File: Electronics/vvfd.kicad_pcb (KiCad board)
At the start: 2 copper layers, 95 x 95 mm, 70 parts, among them J1 USB_C_Receptacle_USB2.0_14P, J2 Conn_01x02_Pin, J3 Conn_02x05_Counter_Clockwise, J4 Conn_02x05_Counter_Clockwise, J5 Conn_02x05_Counter_Clockwise, J6 Conn_01x08_Pin, J7 Conn_01x08_Pin, J8 Conn_01x08_Pin, J9 Conn_01x08_Pin, Q1 RFD14N05L, Q2 RFD14N05L, Q3 RFD14N05L, Q4 RFD14N05L, Q5 RFD14N05L, Q6 RFD14N05L, U1 MC34063AD, U10 TBD62783A, U2 TLV274, U3 74HC595, U4 TBD62783A, U5 74HC595, U6 TBD62783A, U7 74HC595, U8 TBD62783A, U9 74HC595

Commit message: Fixed ERC and DRC
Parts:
- Q1, Q2, Q3, Q4, Q5, Q6: value RFD14N05L -> IRLU014PBF

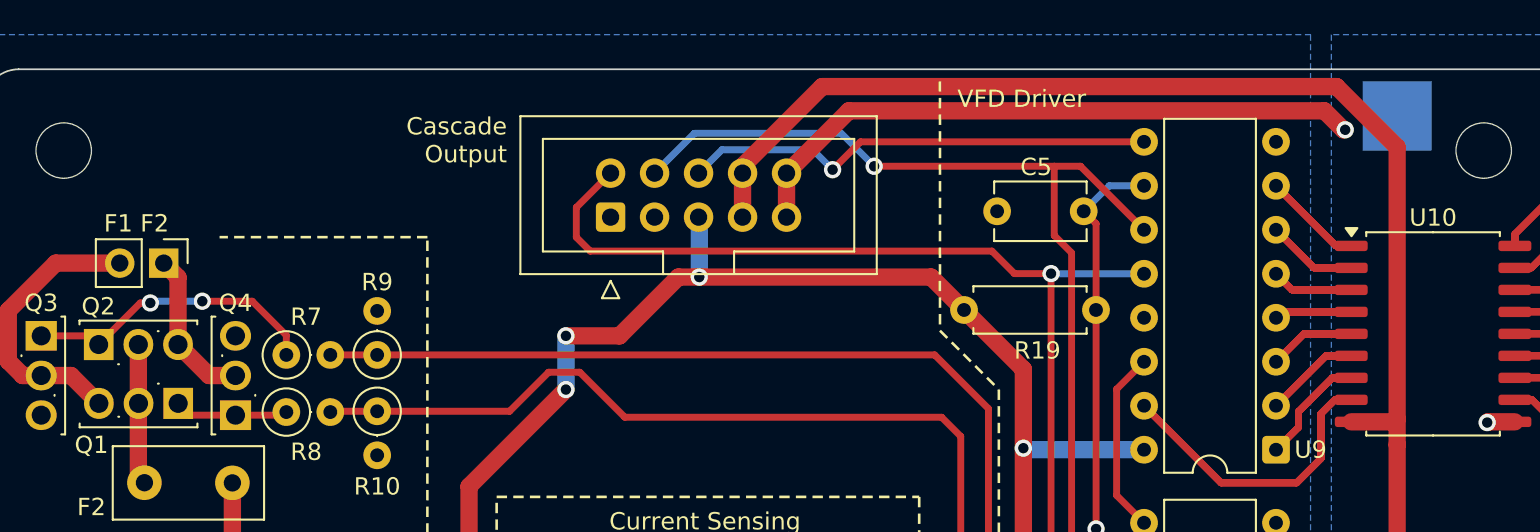
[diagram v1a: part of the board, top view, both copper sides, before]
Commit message: Fix cascade IDC connector
The cascade input and output IDC pins didn't correspond before
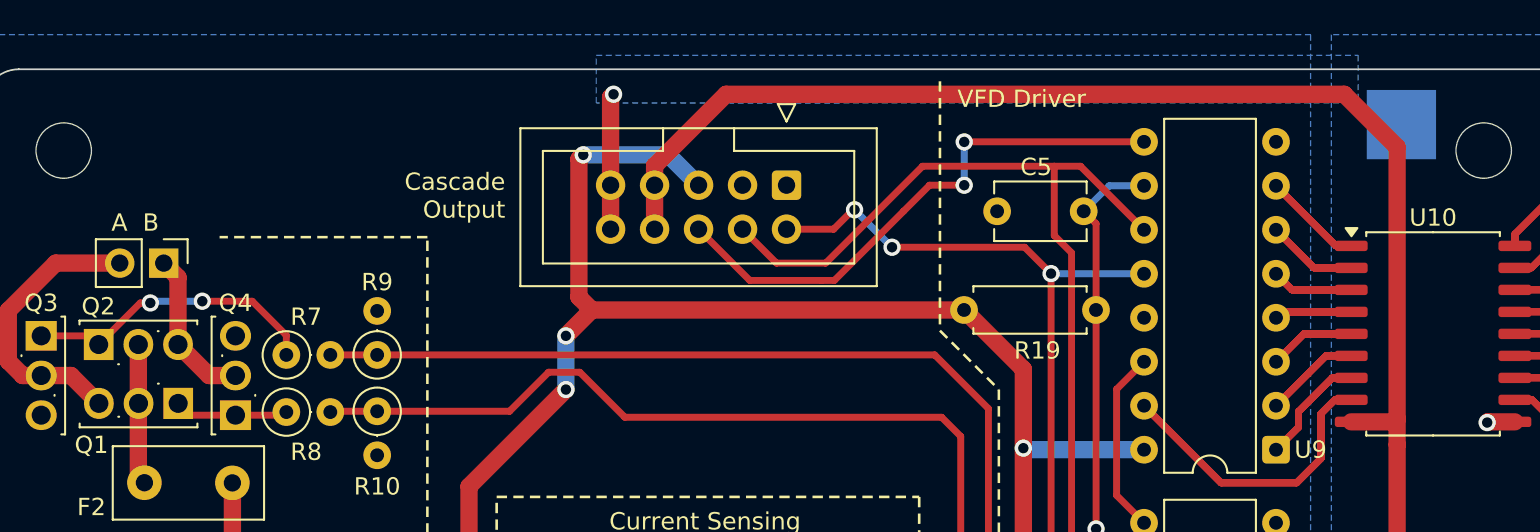
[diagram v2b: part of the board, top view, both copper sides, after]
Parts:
- moved J3 10.3 mm to (159.7, 50.0), turned to -90 degrees
- moved TP3 0.56 mm to (195.2, 46.5)
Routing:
- net GNDA: track 154.4 -> 125.5 mm
- net SYNC: track 155.5 -> 139.9 mm, vias 1 -> 3
- net VCC: track 204.5 -> 216.2 mm
- net VDC: track 232.5 -> 237.7 mm
- net MAIN_SER_OUT: track 27.4 -> 31.7 mm, vias 1 -> 2
- net CLK: track 152.3 -> 148.6 mm, vias 7 -> 6
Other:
- board text added: "A B"
- board text removed: "F1 F2"

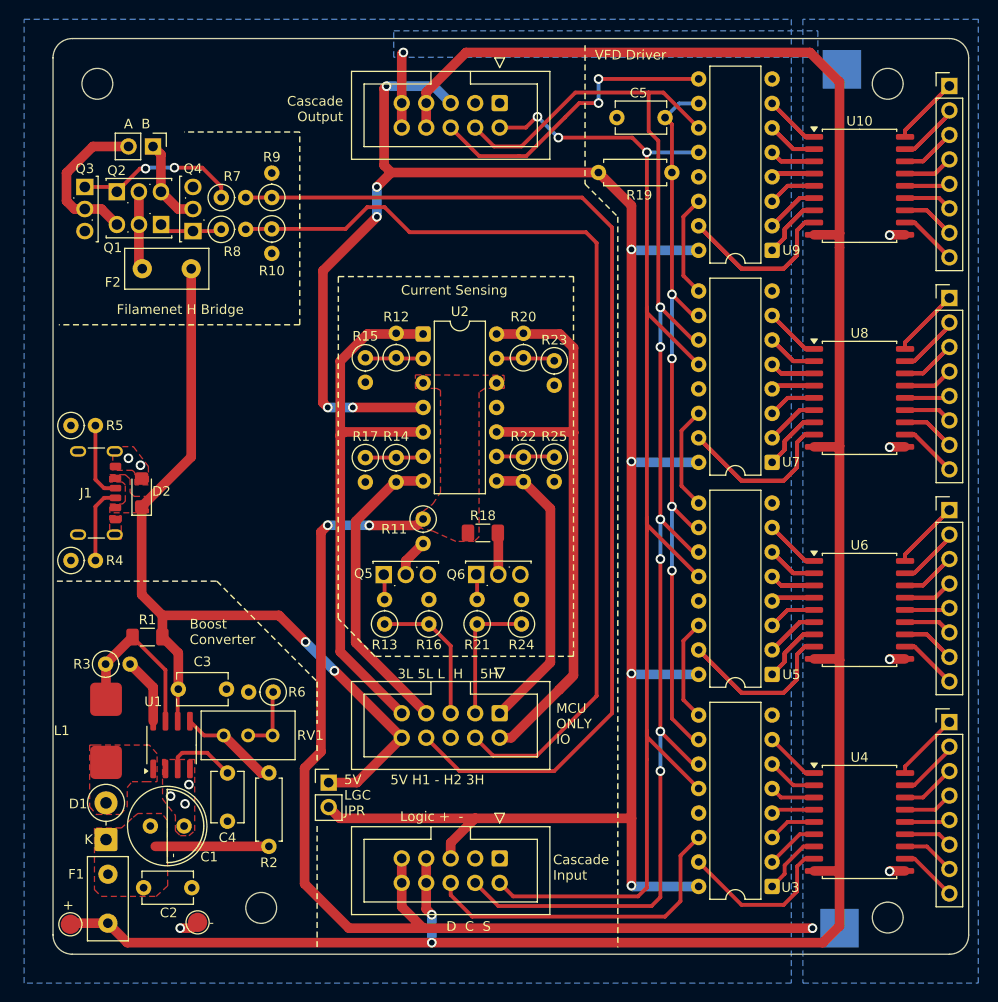
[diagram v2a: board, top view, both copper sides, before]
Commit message: Added filament timer
Added a timer to control the filament h-brdige on the main PCB.
Also added some more decoupling capacitors, but some have dubious
placement. Still better than nothing.
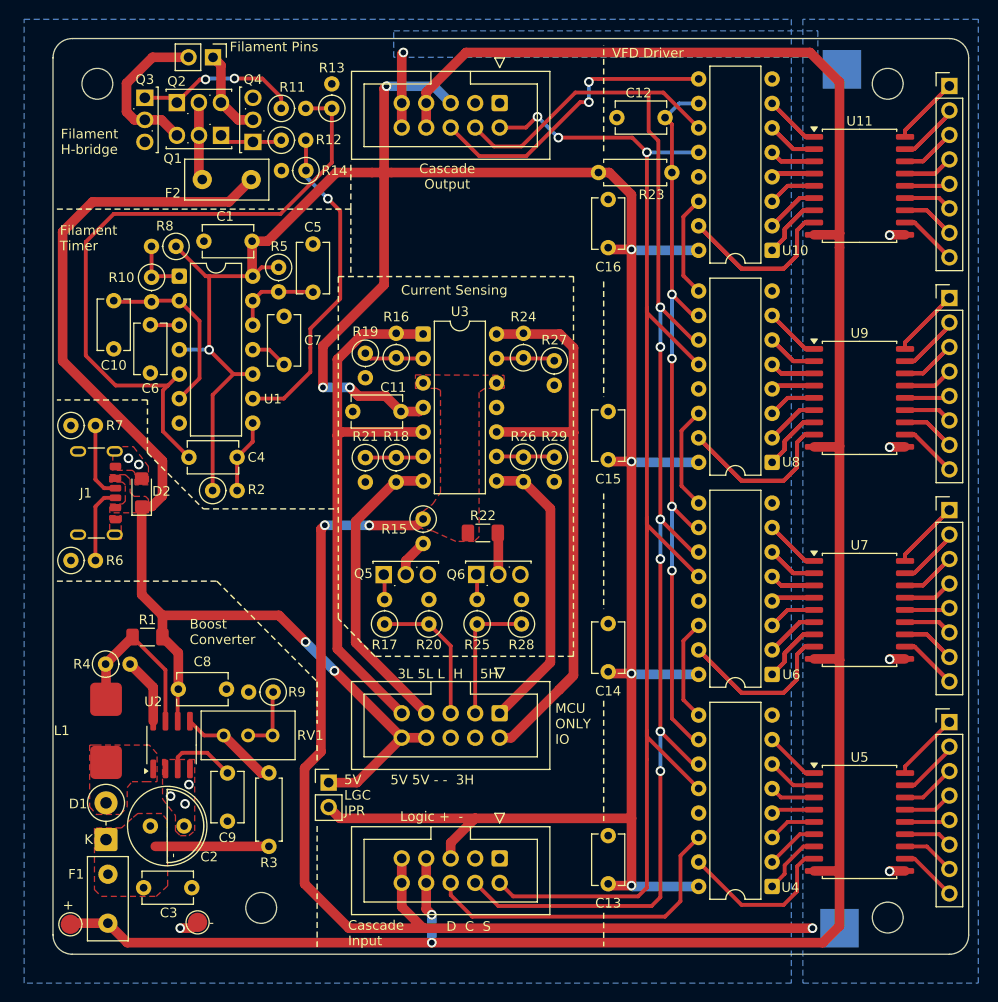
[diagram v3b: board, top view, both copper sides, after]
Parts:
- added C1: 100n, Capacitor_THT:C_Disc_D5.1mm_W3.2mm_P5.00mm, F.Cu at (134.1, 64.3)
- added C10: 220n, Capacitor_THT:C_Disc_D5.1mm_W3.2mm_P5.00mm, F.Cu at (119.7, 70.5)
- added C11: 100n, Capacitor_THT:C_Disc_D5.1mm_W3.2mm_P5.00mm, F.Cu at (149.5, 82.0)
- added C13: 100n, Capacitor_THT:C_Disc_D5.1mm_W3.2mm_P5.00mm, F.Cu at (171.0, 131.0)
- added C14: 100n, Capacitor_THT:C_Disc_D5.1mm_W3.2mm_P5.00mm, F.Cu at (171.0, 109.0)
- added C15: 100n, Capacitor_THT:C_Disc_D5.1mm_W3.2mm_P5.00mm, F.Cu at (171.0, 87.0)
- added C16: 100n, Capacitor_THT:C_Disc_D5.1mm_W3.2mm_P5.00mm, F.Cu at (171.0, 65.0)
- added C4: 1n, Capacitor_THT:C_Disc_D5.1mm_W3.2mm_P5.00mm, F.Cu at (127.5, 86.8)
- added C5: 220n, Capacitor_THT:C_Disc_D5.1mm_W3.2mm_P5.00mm, F.Cu at (140.4, 69.6)
- added C6: 10n, Capacitor_THT:C_Disc_D5.1mm_W3.2mm_P5.00mm, F.Cu at (123.5, 73.0)
- added C7: 10n, Capacitor_THT:C_Disc_D5.1mm_W3.2mm_P5.00mm, F.Cu at (137.4, 77.1)
- added R10: 68k, Resistor_THT:R_Axial_DIN0207_L6.3mm_D2.5mm_P2.54mm_Vertical, F.Cu at (123.6, 68.1)
- added R2: 33k, Resistor_THT:R_Axial_DIN0207_L6.3mm_D2.5mm_P2.54mm_Vertical, F.Cu at (130.0, 90.2)
- added R5: 39k, Resistor_THT:R_Axial_DIN0207_L6.3mm_D2.5mm_P2.54mm_Vertical, F.Cu at (136.8, 67.0)
- added R8: 1k, Resistor_THT:R_Axial_DIN0207_L6.3mm_D2.5mm_P2.54mm_Vertical, F.Cu at (126.2, 64.9)
- added U1: LM556, Package_DIP:DIP-14_W7.62mm, F.Cu at (126.5, 68.0)
- moved R11 11.1 mm to (137.1, 50.5)
- moved R12 11.1 mm to (137.1, 53.9)
- moved F2 11.1 mm to (134.0, 57.9)
- moved Q1 11.1 mm to (130.8, 53.4)
- moved Q2 11.1 mm to (126.2, 50.0)
- moved Q4 11.1 mm to (134.1, 54.0)
- moved J2 11.1 mm to (130.0, 45.2)
- moved Q3 11.1 mm to (122.9, 49.5)
- moved R13 11.1 mm to (142.3, 50.5)
- moved R14 7.02 mm to (139.6, 57.0), turned to 180 degrees
- moved R19 0.47 mm to (145.8, 76.0)
- renumbered C5 to C12, C1 to C2, C2 to C3, C3 to C8, C4 to C9, J5 to J4, J4 to J5, R7 to R11, R8 to R12, R9 to R13, R10 to R14, R11 to R15, R12 to R16, R13 to R17, R14 to R18, R15 to R19, R16 to R20, R17 to R21, R18 to R22, R19 to R23, R20 to R24, R21 to R25, R22 to R26, R23 to R27, R24 to R28, R25 to R29, R2 to R3, R3 to R4, R4 to R6, R5 to R7, R6 to R9, TP3 to TP1, TP4 to TP2, TP2 to TP3, TP1 to TP4, U9 to U10, U10 to U11, U1 to U2, U2 to U3, U3 to U4, U4 to U5, U5 to U6, U6 to U7, U7 to U8, U8 to U9
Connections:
- J4 pad 4: H2 -> GND
- J4 pad 8: H1 -> +5V
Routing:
- net VCC: track 216.2 -> 288.3 mm, vias 9 -> 8
- net H2: track 101.8 -> 34.0 mm, vias 0 -> 1
- net H1: track 112.9 -> 69.3 mm
- net +5V: track 90.5 -> 122.3 mm
- net /TIMING_CAP_1: track 0.00 -> 18.8 mm
- net /TIMING_CAP_2: track 0.00 -> 9.19 mm
- net /TIM_2_IN: track 0.00 -> 7.67 mm
- net /TIM_1_DIS: track 0.00 -> 6.13 mm
- net /TIM_2_CV: track 0.00 -> 3.89 mm
- net /TIM_1_CV: track 0.00 -> 3.02 mm
- net 3LCS: track 57.8 -> 58.6 mm
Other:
- board text added: "5V 5V - - 3H"
- board text added: "Filament H-bridge"
- board text added: "Filament Pins"
- board text added: "Filament Timer"
- board text removed: "5V H1 - H2 3H"
- board text removed: "A B"
- board text removed: "Filamenet H Bridge"

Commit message: Added VFD output pulldowns
Added pulldowns and more decoupling capacitors. The capacitors and
pulldowns can probably be omitted, but I've put them in for more flexibility.
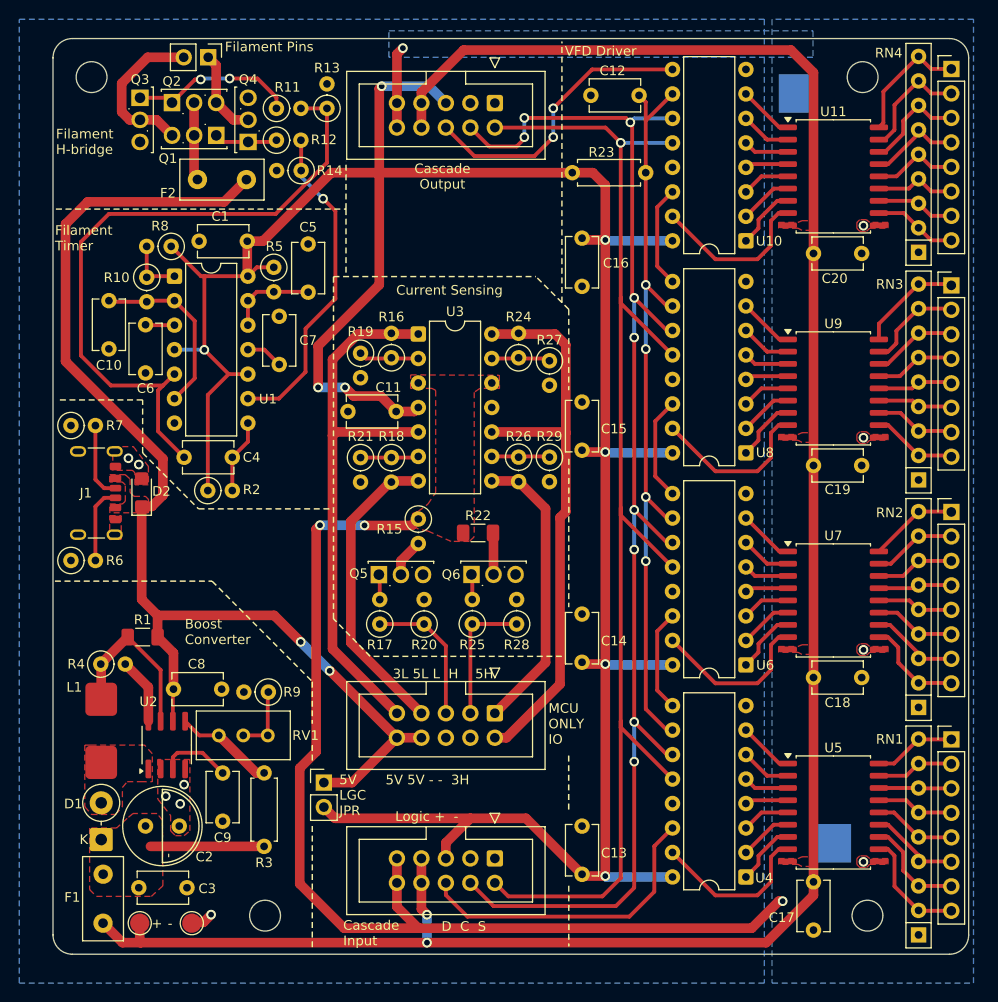
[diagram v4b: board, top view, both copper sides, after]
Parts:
- added C17: 100n, Capacitor_THT:C_Disc_D5.1mm_W3.2mm_P5.00mm, F.Cu at (192.3, 130.8)
- added C18: 100n, Capacitor_THT:C_Disc_D5.1mm_W3.2mm_P5.00mm, F.Cu at (192.3, 109.6)
- added C19: 100n, Capacitor_THT:C_Disc_D5.1mm_W3.2mm_P5.00mm, F.Cu at (192.3, 87.6)
- added C20: 100n, Capacitor_THT:C_Disc_D5.1mm_W3.2mm_P5.00mm, F.Cu at (192.3, 65.6)
- added RN1: 1M, Resistor_THT:R_Array_SIP9, F.Cu at (203.2, 136.3)
- added RN2: 1M, Resistor_THT:R_Array_SIP9, F.Cu at (203.2, 112.7)
- added RN3: 1M, Resistor_THT:R_Array_SIP9, F.Cu at (203.2, 89.1)
- added RN4: 1M, Resistor_THT:R_Array_SIP9, F.Cu at (203.2, 65.5)
- moved TP2 8.84 mm to (194.2, 126.8)
- moved TP4 7.20 mm to (122.4, 135.1)
- moved TP1 5.19 mm to (190.7, 49.0)
- moved C12 3.55 mm to (174.2, 49.2)
- moved C13 2.89 mm to (168.3, 130.0)
- moved U4 2.89 mm to (185.3, 130.3)
- moved C14 2.89 mm to (168.3, 108.0)
- moved C15 2.89 mm to (168.3, 86.0)
- moved C16 2.89 mm to (168.3, 64.0), turned to -90 degrees
- moved U10 2.89 mm to (185.3, 64.3)
- moved U6 2.89 mm to (185.3, 108.3)
- moved U8 2.89 mm to (185.3, 86.3)
- moved U11 2.89 mm to (194.4, 57.6)
- moved U5 2.89 mm to (194.4, 123.6)
- moved U7 2.89 mm to (194.4, 101.6)
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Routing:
- net /VFD drive 2/A: track 51.9 -> 17.3 mm
- net /VFD drive 3/A: track 51.9 -> 17.3 mm
- net /VFD drive 4/A: track 51.9 -> 17.3 mm
- net VDC: track 237.7 -> 219.9 mm
- net /VFD drive 3/B: track 19.8 -> 6.59 mm
- net /VFD drive 2/B: track 19.8 -> 6.59 mm
- net /VFD drive 4/B: track 19.8 -> 6.59 mm
- net /VFD drive 4/H: track 17.3 -> 5.78 mm
- net /VFD drive 3/H: track 17.3 -> 5.78 mm
- net /VFD drive 2/H: track 17.3 -> 5.78 mm
- net CLK: track 148.6 -> 137.3 mm, vias 6 -> 9
- net /VFD drive 4/C: track 16.6 -> 5.54 mm
- net /VFD drive 3/C: track 16.6 -> 5.54 mm
- net /VFD drive 2/C: track 16.6 -> 5.54 mm
- net /VFD drive 3/G: track 15.8 -> 5.26 mm
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- added copper zone on F.Cu, net VDC

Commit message: Fixed H-bridge
Old H-bridge was the wrong type, changed to using some P-channel
mosfets. Also fixed the cost spreadsheet.
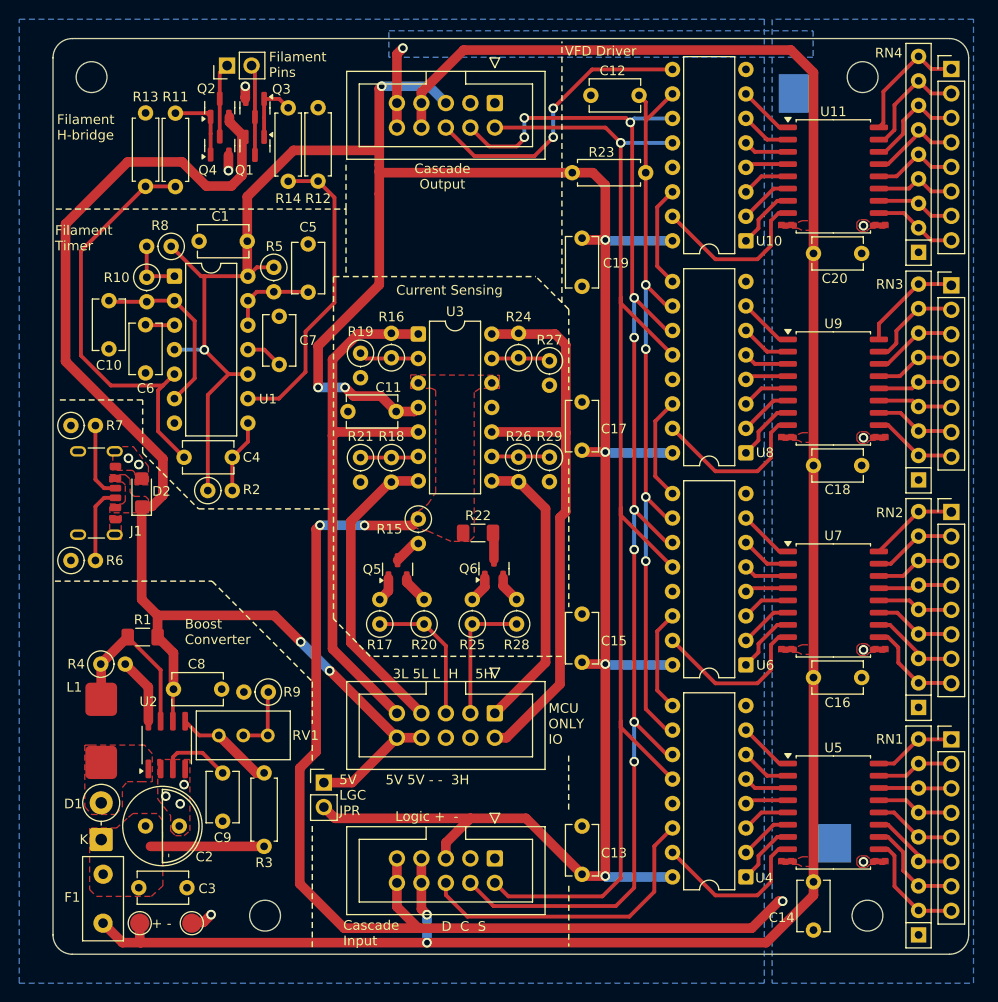
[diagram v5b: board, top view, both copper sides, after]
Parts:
- removed F2: 500mA hold, Fuse:Fuse_Littelfuse_395Series
- Q1, Q2: value IRLU014PBF -> DMG2305UX; footprint Package_TO_SOT_THT:TO-251-3_Vertical -> Package_TO_SOT_SMD:SOT-23
- Q3, Q4, Q5, Q6: value IRLU014PBF -> SL3402; footprint Package_TO_SOT_THT:TO-251-3_Vertical -> Package_TO_SOT_SMD:SOT-23
- R11, R12, R13, R14: footprint Resistor_THT:R_Axial_DIN0207_L6.3mm_D2.5mm_P2.54mm_Vertical -> Resistor_THT:R_Axial_DIN0207_L6.3mm_D2.5mm_P7.62mm_Horizontal
- moved R13 20.5 mm to (123.0, 58.6)
- moved Q3 12.0 mm to (134.3, 50.5)
- moved R11 10.5 mm to (126.1, 51.0), turned to -90 degrees
- moved Q2 4.98 mm to (130.7, 50.5), turned to 90 degrees
- moved Q1 4.16 mm to (134.3, 54.4), turned to -90 degrees
- moved R12 3.57 mm to (137.8, 50.5), turned to -90 degrees
- moved Q4 2.97 mm to (130.7, 54.4)
- moved Q6 2.42 mm to (159.2, 98.3), turned to 90 degrees
- moved J2 2.14 mm to (131.5, 46.1), turned to 90 degrees
- moved R14 2.07 mm to (140.9, 58.1), turned to 90 degrees
- moved Q5 2.02 mm to (149.2, 98.4), turned to 90 degrees
- renumbered C17 to C14, C14 to C15, C18 to C16, C15 to C17, C19 to C18, C16 to C19
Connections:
- Q1 pad 2: /H_BRIDGE_5V -> +5V
- Q2 pad 2: /H_BRIDGE_5V -> +5V
- Q3 pad 1: BRIDGE_G1 -> BRIDGE_G2
- Q3 pad 2: FILAMENT_1 -> GND
- Q3 pad 3: GND -> FILAMENT_1
- Q4 pad 1: BRIDGE_G2 -> BRIDGE_G1
- Q4 pad 2: FILAMENT_2 -> GND
- Q4 pad 3: GND -> FILAMENT_2
- Q5 pad 2: /LCS_DRAIN -> GND
- Q5 pad 3: GND -> /LCS_DRAIN
- Q6 pad 2: /HCS_DRAIN -> GND
- Q6 pad 3: GND -> /HCS_DRAIN
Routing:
- net H1: track 69.3 -> 43.7 mm
- net BRIDGE_G1: track 16.6 -> 7.73 mm, vias 2 -> 0
- net GND: track 2.23 -> 10.9 mm, vias 6 -> 8
- net +5V: track 121.4 -> 129.8 mm
- net /H_BRIDGE_5V: track 7.63 -> 0.00 mm
- net FILAMENT_1: track 16.8 -> 9.42 mm
- net VCC: track 282.3 -> 286.0 mm
- net H2: track 33.9 -> 32.0 mm, vias 1 -> 0
- net /HCS_DRAIN: track 4.25 -> 2.81 mm
- net FILAMENT_2: track 9.10 -> 7.68 mm
- net /LCS_DRAIN: track 3.98 -> 2.87 mm

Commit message: Updated BOM
Updated BOMs because some of the component prices changed and a part
went out of stock.
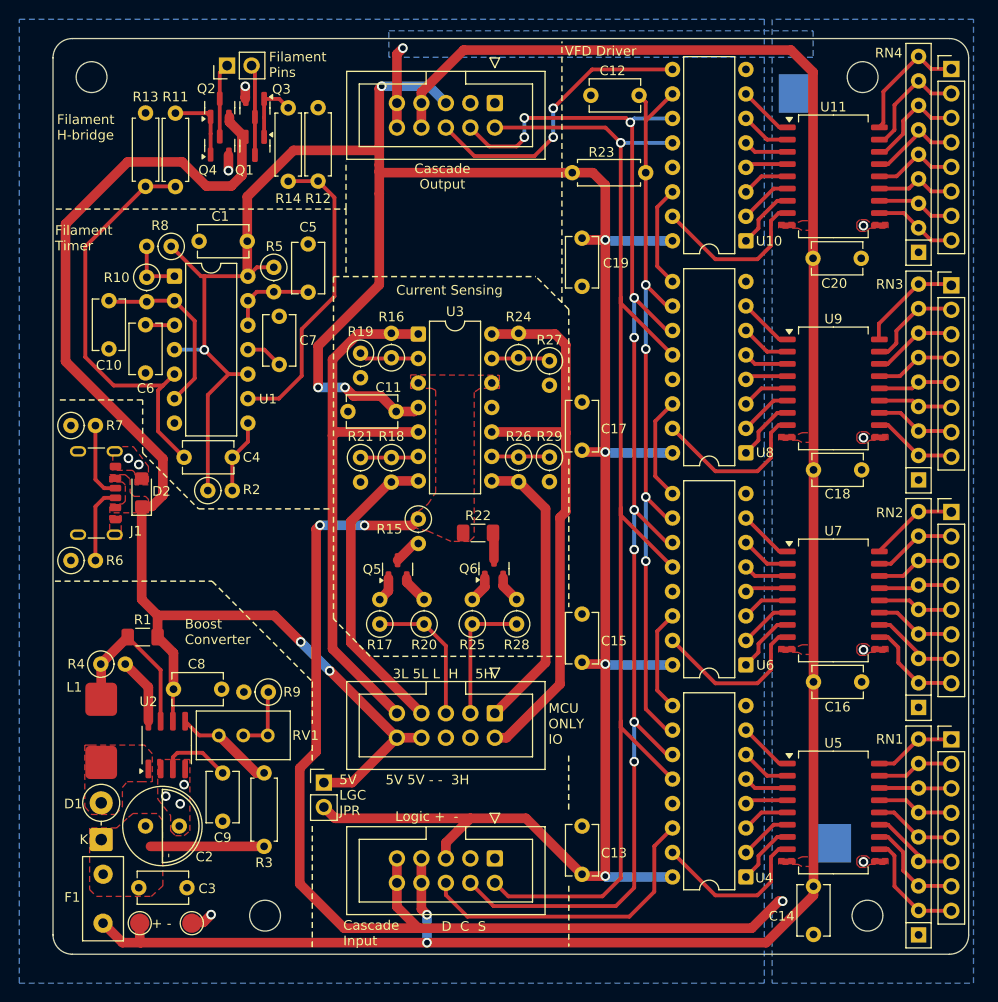
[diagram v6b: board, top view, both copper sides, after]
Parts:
- U11, U5, U7, U9: footprint Custom:SOP-18_7.495x11.515mm_P1.27mm -> Package_SO:SOP-18_7x12.5mm_P1.27mm
- moved C20 0.51 mm to (192.2, 66.1)
- moved C16 0.46 mm to (192.3, 110.1)
- moved C18 0.46 mm to (192.3, 88.1)
- moved C14 0.45 mm to (192.3, 131.3)
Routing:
- net H1: track 43.7 -> 43.1 mm
